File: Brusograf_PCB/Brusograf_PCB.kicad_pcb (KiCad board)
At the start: 2 copper layers, 159 x 48.8 mm, 40 parts, among them J1 Conn_01x05_Socket, J2 Conn_01x05_Socket, J3 Conn_01x05_Socket, J4 SD_Card_Receptacle, J5 Barrel_Jack_Switch, J6 Conn_01x07_Socket, J7 Conn_01x03_Pin, J8 Conn_01x01_Socket, U1 ULN2003A, U2 ULN2003A, U3 ULN2003A, U4 ESP32-DevKitC

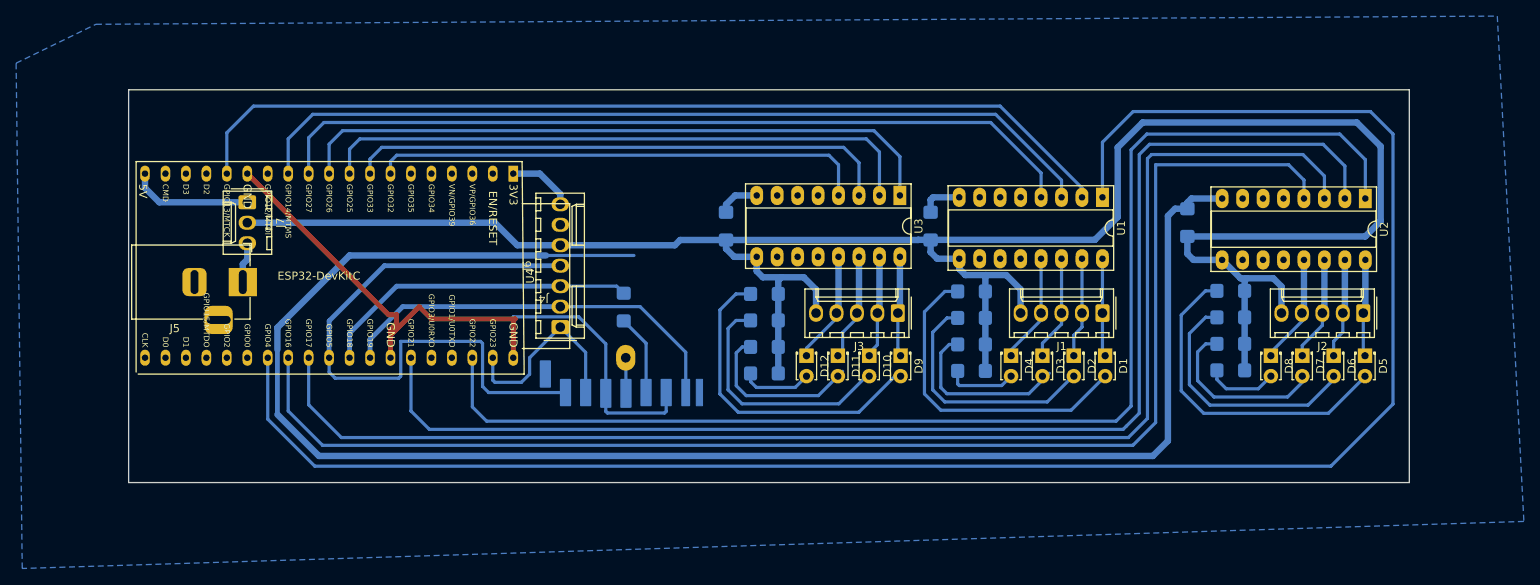
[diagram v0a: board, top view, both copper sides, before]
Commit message: fully manucturable PCB design and gerbers
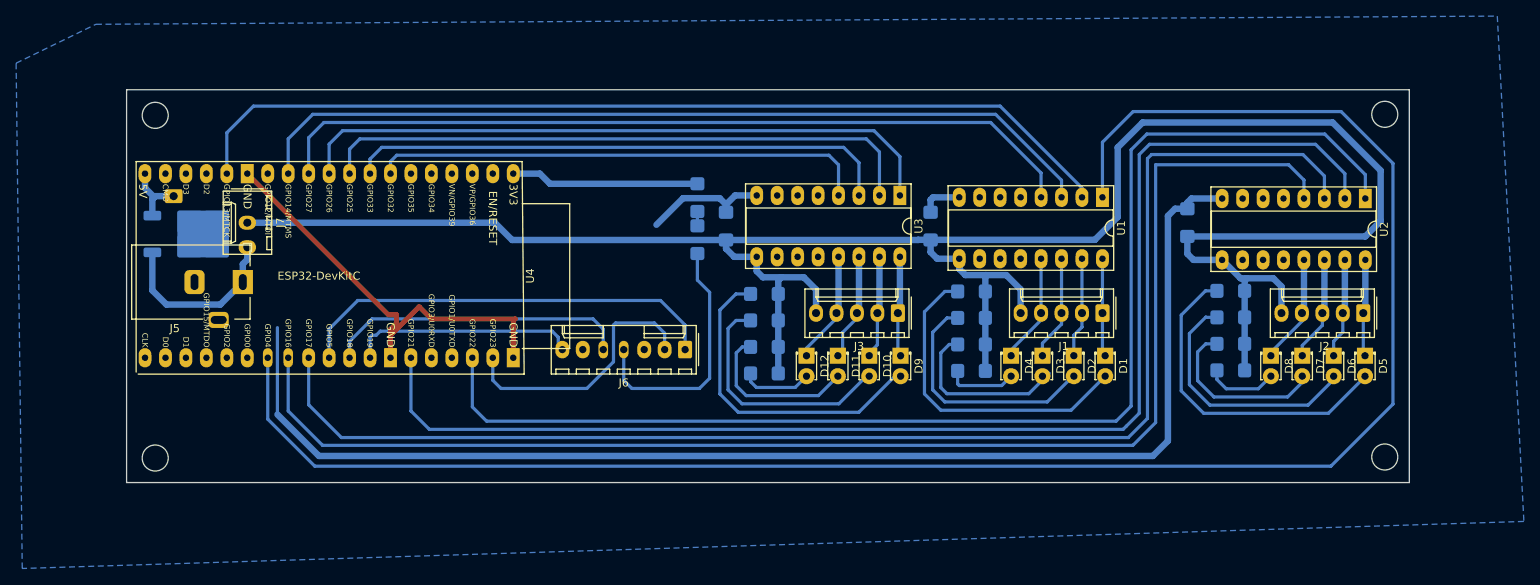
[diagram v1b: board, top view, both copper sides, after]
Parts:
- removed J4: SD_Card_Receptacle, Connector_Card:SD_Card_Device_16mm_SlotDepth
- removed J8: Conn_01x01_Socket, 007_dusjagr:SolderPad_small
- added R14: 0, 007_dusjagr:R_1206_noGND, B.Cu at (116.1, 98.7)
- added U5: L7805, Package_TO_SOT_SMD:TO-252-2, B.Cu at (53.5, 103.3)
- D1, D10, D11, D12, D2, D3, D4, D5, D6, D7, D8, D9: footprint LED_THT:LED_D1.8mm_W3.3mm_H2.4mm -> 007_dusjagr:LED_D1.8mm_W3.3mm_H2.4mm
- J1, J2, J3: footprint Connector_Molex:Molex_KK-254_AE-6410-05A_1x05_P2.54mm_Vertical -> 007_dusjagr:Molex_1x05_P2.54mm_Vertical
- J6: footprint Connector_Molex:Molex_KK-254_AE-6410-07A_1x07_P2.54mm_Vertical -> 007_dusjagr:Molex_KK-254_AE-6410-07A_1x07_P2.54mm_Vertical
- U4: footprint PCM_Espressif:ESP32-DevKitC -> 007_dusjagr:ESP32-DevKitC_mod
- moved J6 15.7 mm to (114.6, 117.6), turned to 180 degrees
- moved R13 12.4 mm to (116.1, 104.0)
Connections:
- J6 pad 1: MOSI -> CS
- J6 pad 2: MISO -> MOSI
- J6 pad 3: SCK -> GND
- J6 pad 4: CS -> Net-(J6-Pin_4)
- J6 pad 5: 5V -> SCK
- J6 pad 7: 3.3V -> MISO
- R13 pad 1: SCK -> Net-(R13-Pad1)
- R13 pad 2: Net-(J4-CLK) -> Net-(J6-Pin_4)
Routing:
- net GND: track 311.8 -> 238.1 mm
- net Net-(J6-Pin_4): track 0.00 -> 31.5 mm
- net CS: track 77.7 -> 53.5 mm
- net MISO: track 50.5 -> 28.3 mm
- net 5V-EXT: track 5.06 -> 22.9 mm
- net 3.3V: track 8.16 -> 23.4 mm
- net Net-(J4-CLK): track 10.0 -> 0.00 mm
- net MOSI: track 24.7 -> 33.2 mm
- net Net-(J7-Pin_1): track 15.2 -> 8.25 mm
- net Net-(J4-VDD): track 4.43 -> 0.00 mm
- net 5V: track 279.0 -> 276.7 mm
- net IN1_U1: track 232.1 -> 230.0 mm
- net SCK: track 39.9 -> 37.8 mm
- net Net-(R13-Pad1): track 0.00 -> 1.78 mm
- net IN1_U2: track 157.3 -> 156.2 mm
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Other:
- board size 159 x 48.8 mm -> 159.3 x 48.8 mm
